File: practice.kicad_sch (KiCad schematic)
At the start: 4 parts, among them M1 PMOS_OR1, M2 NMOS_OR1, M3 PMOS_OR1, M4 NMOS_OR1

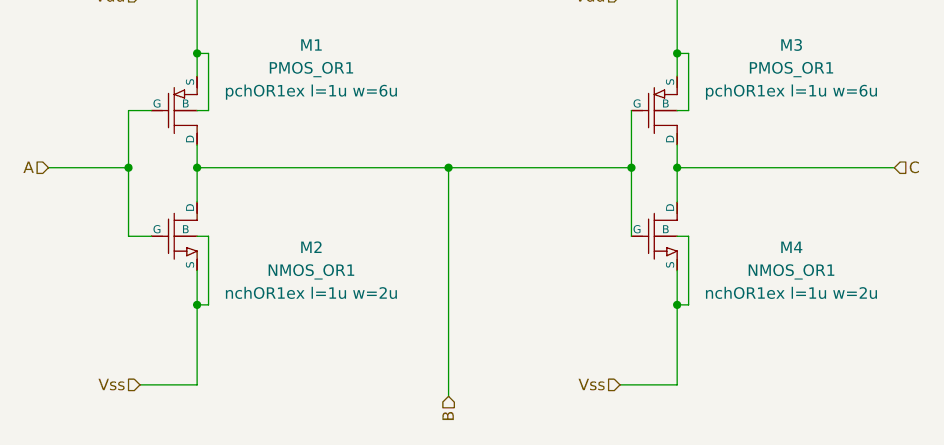
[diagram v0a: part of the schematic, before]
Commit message: 入出力点を双方向に変更
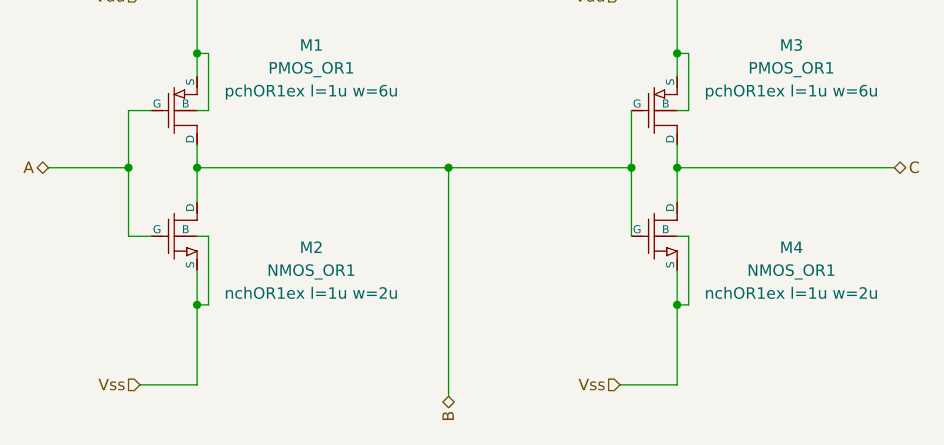
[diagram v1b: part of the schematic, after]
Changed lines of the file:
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@@
     (effects (font (size 1.27 1.27)) (justify right))
   )
-  (hierarchical_label "A" (shape input) (at 69.85 67.31 180)
+  (hierarchical_label "A" (shape bidirectional) (at 69.85 67.31 180)
     (effects (font (size 1.27 1.27)) (justify right))
   )
-  (hierarchical_label "B" (shape input) (at 114.3 92.71 270)
+  (hierarchical_label "B" (shape bidirectional) (at 114.3 92.71 270)
     (effects (font (size 1.27 1.27)) (justify right))
   )
@@
     (effects (font (size 1.27 1.27)) (justify right))
   )
-  (hierarchical_label "C" (shape input) (at 163.83 67.31 0)
+  (hierarchical_label "C" (shape bidirectional) (at 163.83 67.31 0)
     (effects (font (size 1.27 1.27)) (justify left))
   )

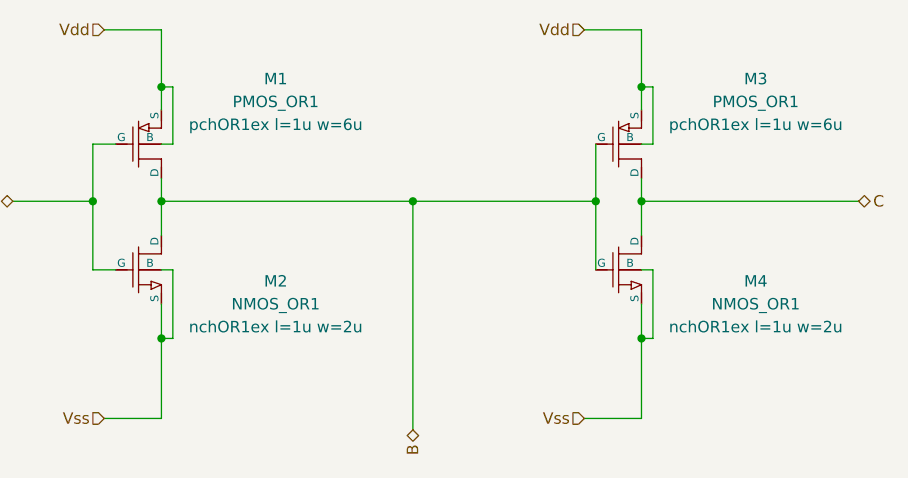
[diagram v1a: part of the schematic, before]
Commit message: 19用に合わせた発振回路
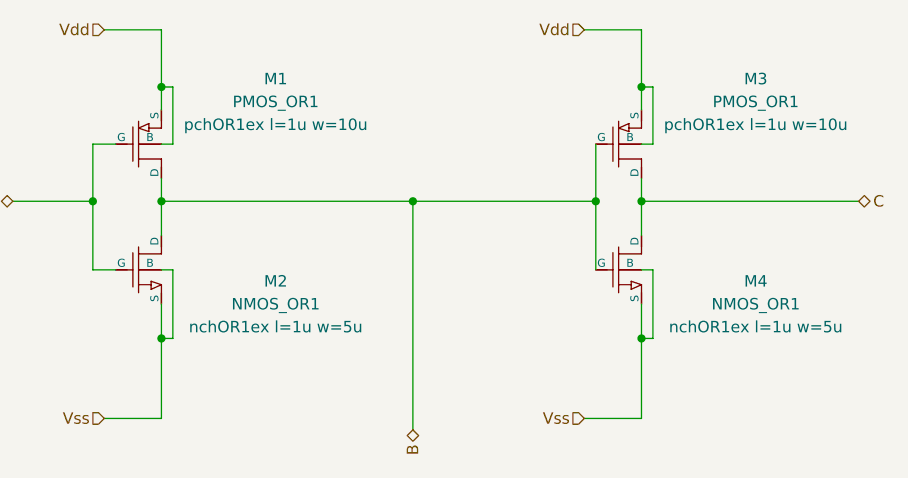
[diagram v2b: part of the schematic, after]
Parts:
- M1, M3: Spice_Model pchOR1ex l=1u w=6u -> pchOR1ex l=1u w=10u
- M2, M4: Spice_Model nchOR1ex l=1u w=2u -> nchOR1ex l=1u w=5u
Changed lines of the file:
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@@
       (effects (font (size 1.27 1.27)) (justify left) hide)
     )
-    (property "Spice_Model" "pchOR1ex l=1u w=6u" (id 5) (at 152.4 58.801 0))
+    (property "Spice_Model" "pchOR1ex l=1u w=10u" (id 5) (at 152.4 58.801 0))
     (property "Spice_Netlist_Enabled" "Y" (id 6) (at 143.51 63.5 0)
       (effects (font (size 1.27 1.27)) (justify left) hide)
@@
       (effects (font (size 1.27 1.27)) (justify left) hide)
     )
-    (property "Spice_Model" "pchOR1ex l=1u w=6u" (id 5) (at 99.06 58.801 0))
+    (property "Spice_Model" "pchOR1ex l=1u w=10u" (id 5) (at 99.06 58.801 0))
     (property "Spice_Netlist_Enabled" "Y" (id 6) (at 90.17 63.5 0)
       (effects (font (size 1.27 1.27)) (justify left) hide)
@@
       (effects (font (size 1.27 1.27)) (justify left) hide)
     )
-    (property "Spice_Model" "nchOR1ex l=1u w=2u" (id 5) (at 99.06 81.28 0))
+    (property "Spice_Model" "nchOR1ex l=1u w=5u" (id 5) (at 99.06 81.28 0))
     (property "Spice_Netlist_Enabled" "Y" (id 6) (at 90.17 77.47 0)
       (effects (font (size 1.27 1.27)) (justify left) hide)
@@
       (effects (font (size 1.27 1.27)) (justify left) hide)
     )
-    (property "Spice_Model" "nchOR1ex l=1u w=2u" (id 5) (at 152.4 81.28 0))
+    (property "Spice_Model" "nchOR1ex l=1u w=5u" (id 5) (at 152.4 81.28 0))
     (property "Spice_Netlist_Enabled" "Y" (id 6) (at 143.51 77.47 0)
       (effects (font (size 1.27 1.27)) (justify left) hide)

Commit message: w,lを変更
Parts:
- M1, M3: Spice_Model pchOR1ex l=1u w=10u -> pchOR1ex l=1u w=12u
- M2, M4: Spice_Model nchOR1ex l=1u w=5u -> nchOR1ex l=1u w=4u
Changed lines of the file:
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@@
       (effects (font (size 1.27 1.27)) (justify left) hide)
     )
-    (property "Spice_Model" "pchOR1ex l=1u w=10u" (id 5) (at 152.4 58.801 0))
+    (property "Spice_Model" "pchOR1ex l=1u w=12u" (id 5) (at 152.4 58.801 0))
     (property "Spice_Netlist_Enabled" "Y" (id 6) (at 143.51 63.5 0)
       (effects (font (size 1.27 1.27)) (justify left) hide)
@@
       (effects (font (size 1.27 1.27)) (justify left) hide)
     )
-    (property "Spice_Model" "pchOR1ex l=1u w=10u" (id 5) (at 99.06 58.801 0))
+    (property "Spice_Model" "pchOR1ex l=1u w=12u" (id 5) (at 99.06 58.801 0))
     (property "Spice_Netlist_Enabled" "Y" (id 6) (at 90.17 63.5 0)
       (effects (font (size 1.27 1.27)) (justify left) hide)
@@
       (effects (font (size 1.27 1.27)) (justify left) hide)
     )
-    (property "Spice_Model" "nchOR1ex l=1u w=5u" (id 5) (at 99.06 81.28 0))
+    (property "Spice_Model" "nchOR1ex l=1u w=4u" (id 5) (at 99.06 81.28 0))
     (property "Spice_Netlist_Enabled" "Y" (id 6) (at 90.17 77.47 0)
       (effects (font (size 1.27 1.27)) (justify left) hide)
@@
       (effects (font (size 1.27 1.27)) (justify left) hide)
     )
-    (property "Spice_Model" "nchOR1ex l=1u w=5u" (id 5) (at 152.4 81.28 0))
+    (property "Spice_Model" "nchOR1ex l=1u w=4u" (id 5) (at 152.4 81.28 0))
     (property "Spice_Netlist_Enabled" "Y" (id 6) (at 143.51 77.47 0)
       (effects (font (size 1.27 1.27)) (justify left) hide)

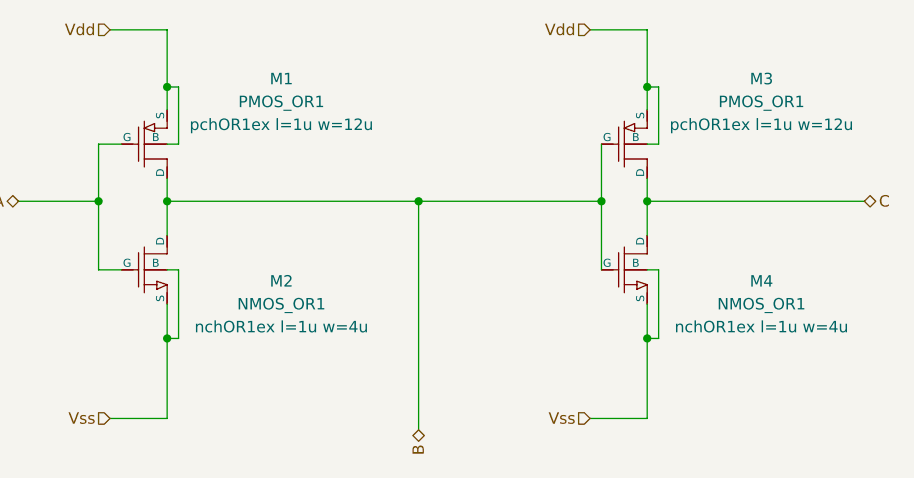
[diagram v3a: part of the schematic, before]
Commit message: マルチフィンガーにせず設計
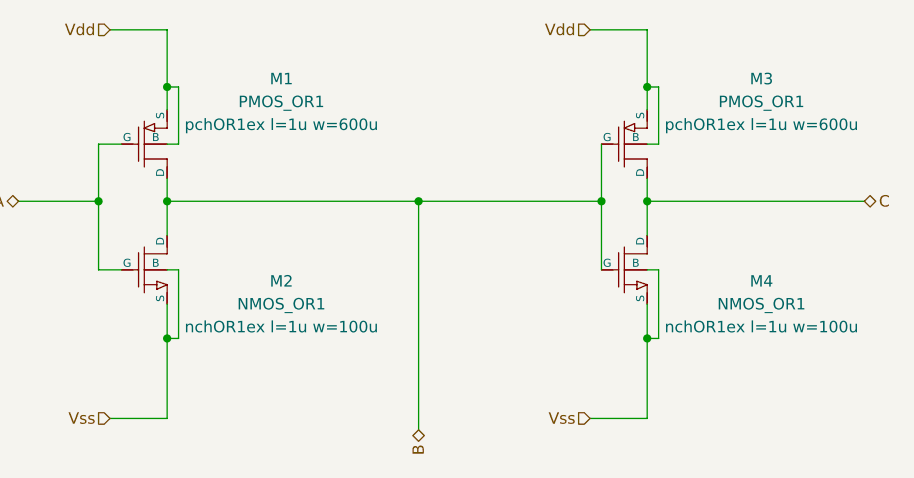
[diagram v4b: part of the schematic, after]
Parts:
- M1, M3: Spice_Model pchOR1ex l=1u w=12u -> pchOR1ex l=1u w=600u
- M2, M4: Spice_Model nchOR1ex l=1u w=4u -> nchOR1ex l=1u w=100u
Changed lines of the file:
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@@
       (effects (font (size 1.27 1.27)) (justify left) hide)
     )
-    (property "Spice_Model" "pchOR1ex l=1u w=12u" (id 5) (at 152.4 58.801 0))
+    (property "Spice_Model" "pchOR1ex l=1u w=600u" (id 5) (at 152.4 58.801 0))
     (property "Spice_Netlist_Enabled" "Y" (id 6) (at 143.51 63.5 0)
       (effects (font (size 1.27 1.27)) (justify left) hide)
@@
       (effects (font (size 1.27 1.27)) (justify left) hide)
     )
-    (property "Spice_Model" "pchOR1ex l=1u w=12u" (id 5) (at 99.06 58.801 0))
+    (property "Spice_Model" "pchOR1ex l=1u w=600u" (id 5) (at 99.06 58.801 0))
     (property "Spice_Netlist_Enabled" "Y" (id 6) (at 90.17 63.5 0)
       (effects (font (size 1.27 1.27)) (justify left) hide)
@@
       (effects (font (size 1.27 1.27)) (justify left) hide)
     )
-    (property "Spice_Model" "nchOR1ex l=1u w=4u" (id 5) (at 99.06 81.28 0))
+    (property "Spice_Model" "nchOR1ex l=1u w=100u" (id 5) (at 99.06 81.28 0))
     (property "Spice_Netlist_Enabled" "Y" (id 6) (at 90.17 77.47 0)
       (effects (font (size 1.27 1.27)) (justify left) hide)
@@
       (effects (font (size 1.27 1.27)) (justify left) hide)
     )
-    (property "Spice_Model" "nchOR1ex l=1u w=4u" (id 5) (at 152.4 81.28 0))
+    (property "Spice_Model" "nchOR1ex l=1u w=100u" (id 5) (at 152.4 81.28 0))
     (property "Spice_Netlist_Enabled" "Y" (id 6) (at 143.51 77.47 0)
       (effects (font (size 1.27 1.27)) (justify left) hide)

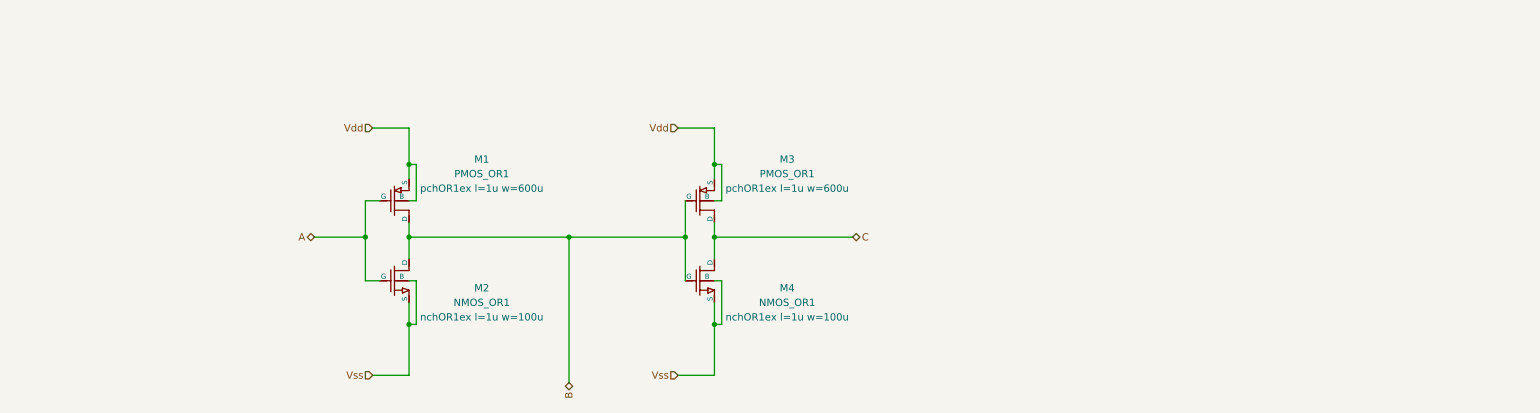
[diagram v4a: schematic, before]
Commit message: マルチフィンガーに設計し直したもの
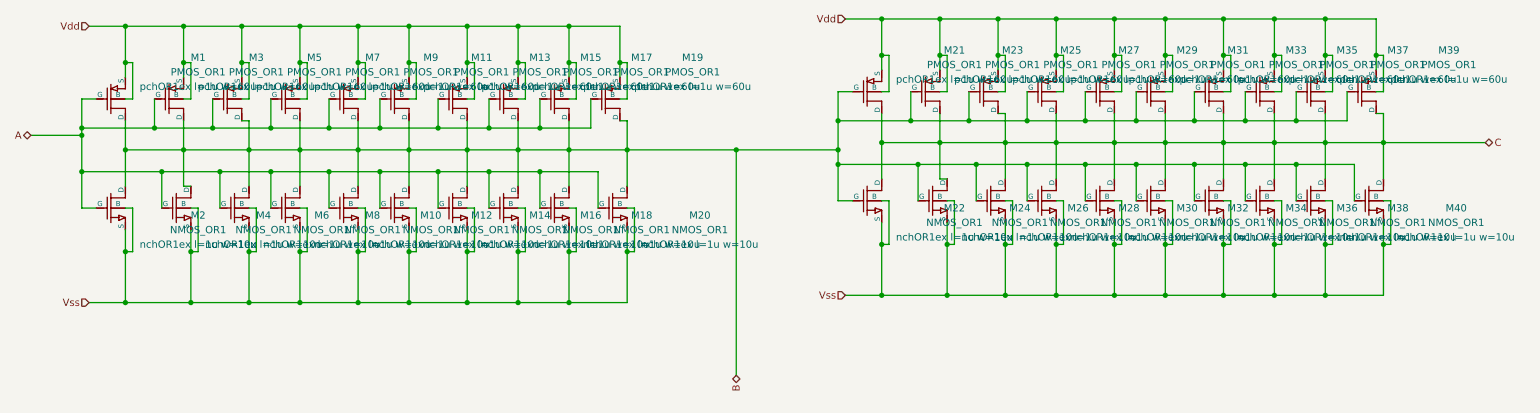
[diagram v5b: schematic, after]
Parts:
- added M10, M12, M14, M16, M18, M20, M22, M24, M26, M28, M30, M32, M34, M36, M38, M40, M6, M8: NMOS_OR1, symbol 0_OR1Symbols:NMOS_OR1
- added M11, M13, M15, M17, M19, M21, M23, M25, M27, M29, M31, M33, M35, M37, M39, M5, M7, M9: PMOS_OR1, symbol 0_OR1Symbols:PMOS_OR1
- M1, M3: Spice_Model pchOR1ex l=1u w=600u -> pchOR1ex l=1u w=60u
- M2, M4: Spice_Model nchOR1ex l=1u w=100u -> nchOR1ex l=1u w=10u
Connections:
- net A: now also M3.2 (G), M4.2 (G), M10.2 (G), M11.2 (G), M12.2 (G), M13.2 (G), M14.2 (G), M15.2 (G), M16.2 (G), M17.2 (G), M18.2 (G), M19.2 (G), M20.2 (G), M5.2 (G), M6.2 (G), M7.2 (G), M8.2 (G), M9.2 (G)
- net B: now also M3.1 (D), M4.1 (D), M10.1 (D), M11.1 (D), M12.1 (D), M13.1 (D), M14.1 (D), M15.1 (D), M16.1 (D), M17.1 (D), M18.1 (D), M19.1 (D), M20.1 (D), M21.2 (G), M22.2 (G), M23.2 (G), M24.2 (G), M25.2 (G), M26.2 (G), M27.2 (G), M28.2 (G), M29.2 (G), M30.2 (G), M31.2 (G), M32.2 (G), M33.2 (G), M34.2 (G), M35.2 (G), M36.2 (G), M37.2 (G), M38.2 (G), M39.2 (G), M40.2 (G), M5.1 (D), M6.1 (D), M7.1 (D), M8.1 (D), M9.1 (D); no longer M3.2 (G), M4.2 (G)
- net C: now also M21.1 (D), M22.1 (D), M23.1 (D), M24.1 (D), M25.1 (D), M26.1 (D), M27.1 (D), M28.1 (D), M29.1 (D), M30.1 (D), M31.1 (D), M32.1 (D), M33.1 (D), M34.1 (D), M35.1 (D), M36.1 (D), M37.1 (D), M38.1 (D), M39.1 (D), M40.1 (D); no longer M3.1 (D), M4.1 (D)
- net Vdd: now also M11.3 (S), M11.4 (B), M13.3 (S), M13.4 (B), M15.3 (S), M15.4 (B), M17.3 (S), M17.4 (B), M19.3 (S), M19.4 (B), M21.3 (S), M21.4 (B), M23.3 (S), M23.4 (B), M25.3 (S), M25.4 (B), M27.3 (S), M27.4 (B), M29.3 (S), M29.4 (B), M31.3 (S), M31.4 (B), M33.3 (S), M33.4 (B), M35.3 (S), M35.4 (B), M37.3 (S), M37.4 (B), M39.3 (S), M39.4 (B), M5.3 (S), M5.4 (B), M7.3 (S), M7.4 (B), M9.3 (S), M9.4 (B)
- net Vss: now also M10.3 (S), M10.4 (B), M12.3 (S), M12.4 (B), M14.3 (S), M14.4 (B), M16.3 (S), M16.4 (B), M18.3 (S), M18.4 (B), M20.3 (S), M20.4 (B), M22.3 (S), M22.4 (B), M24.3 (S), M24.4 (B), M26.3 (S), M26.4 (B), M28.3 (S), M28.4 (B), M30.3 (S), M30.4 (B), M32.3 (S), M32.4 (B), M34.3 (S), M34.4 (B), M36.3 (S), M36.4 (B), M38.3 (S), M38.4 (B), M40.3 (S), M40.4 (B), M6.3 (S), M6.4 (B), M8.3 (S), M8.4 (B)
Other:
- moved on the sheet: M1, M2
